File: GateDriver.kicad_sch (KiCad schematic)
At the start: 9 parts, among them U2 UP1966E

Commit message: added license and almost ready for prod
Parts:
- C38, C39: Rating (none) -> 100V
- C40: Rating (none) -> 6.3V
- R1, R2, R4, R5, R8: Rating (none) -> 100mW
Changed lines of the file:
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@@
+			)
+		)
+		(property "Rating" "100mW"
+			(at 151.13 60.96 0)
+			(effects
+				(font
+					(size 1.27 1.27)
+				)
+				(hide yes)
 			)
 		)
@@
 			)
 		)
+		(property "Rating" "100V"
+			(at 176.53 66.04 0)
+			(effects
+				(font
+					(size 1.27 1.27)
+				)
+				(hide yes)
+			)
+		)
 		(pin "2"
 		)
@@
 		)
 		(property "Description" "Resistor, US symbol"
+			(at 81.28 63.5 0)
+			(effects
+				(font
+					(size 1.27 1.27)
+				)
+				(hide yes)
+			)
+		)
+		(property "Rating" "100mW"
 			(at 81.28 63.5 0)
 			(effects
@@
 			)
 		)
+		(property "Rating" ""
+			(at 92.71 73.66 0)
+			(effects
+				(font
+					(size 1.27 1.27)
+				)
+				(hide yes)
+			)
+		)
 		(pin "A3"
 		)
@@
 			)
 		)
+		(property "Rating" "100V"
+			(at 58.42 72.39 0)
+			(effects
+				(font
+					(size 1.27 1.27)
+				)
+				(hide yes)
+			)
+		)
 		(pin "2"
 		)
@@
 			)
 		)
+		(property "Rating" "100mW"
+			(at 82.55 73.66 0)
+			(effects
+				(font
+					(size 1.27 1.27)
+				)
+				(hide yes)
+			)
+		)
 		(pin "2"
 		)
@@
 		)
 		(property "Description" "Resistor, US symbol"
+			(at 143.51 66.04 0)
+			(effects
+				(font
+					(size 1.27 1.27)
+				)
+				(hide yes)
+			)
+		)
+		(property "Rating" "100mW"
 			(at 143.51 66.04 0)
 			(effects
@@
 			)
 		)
+		(property "Rating" "6.3V"
+			(at 44.45 72.39 0)
+			(effects
+				(font
+					(size 1.27 1.27)
+				)
+				(hide yes)
+			)
+		)
 		(pin "2"
 		)
@@
 			(at 146.05 68.58 0)
 			(effects
+				(font
+					(size 1.27 1.27)
+				)
+				(hide yes)
+			)
+		)
+		(property "Rating" "100mW"
+			(at 146.05 68.58 0)
+			(effects

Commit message: first fab run
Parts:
- C38, C39: Manufacturer_Part_Number (none) -> CGA0603X7R104K500JT; Rating 100V -> 6.3V; Source (none) -> LCSC
- C40: Manufacturer_Part_Number (none) -> V475M0603X5R6R3NDT; Source (none) -> LCSC
- R1, R4: value 0 -> 1; Manufacturer_Part_Number (none) -> FRC0603J1R0 TS; Source (none) -> LCSC
- R2, R5, R8: Manufacturer_Part_Number (none) -> SCR0603J0R; Source (none) -> LCSC
- U2: Manufacturer_Part_Number (none) -> UP1966E; Rating (none) -> 85V; Source (none) -> Digikey
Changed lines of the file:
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@@
 		(company "Crab Labs")
 		(comment 1 "Author: Orion Serup")
+		(comment 2 "License: CERN-OHL-W-2.0")
 	)
 	(junction
@@
 			)
 		)
+		(property "Source" "LCSC"
+			(at 151.13 60.96 0)
+			(effects
+				(font
+					(size 1.27 1.27)
+				)
+				(hide yes)
+			)
+		)
+		(property "Manufacturer_Part_Number" "SCR0603J0R"
+			(at 151.13 60.96 0)
+			(effects
+				(font
+					(size 1.27 1.27)
+				)
+				(hide yes)
+			)
+		)
 		(pin "2"
 		)
@@
 			)
 		)
-		(property "Rating" "100V"
+		(property "Rating" "6.3V"
+			(at 176.53 66.04 0)
+			(effects
+				(font
+					(size 1.27 1.27)
+				)
+				(hide yes)
+			)
+		)
+		(property "Source" "LCSC"
+			(at 176.53 66.04 0)
+			(effects
+				(font
+					(size 1.27 1.27)
+				)
+				(hide yes)
+			)
+		)
+		(property "Manufacturer_Part_Number" "CGA0603X7R104K500JT"
 			(at 176.53 66.04 0)
 			(effects
@@
 			)
 		)
-		(property "Value" "0"
+		(property "Value" "1"
 			(at 84.582 61.976 90)
 			(effects
@@
 		)
 		(property "Rating" "100mW"
+			(at 81.28 63.5 0)
+			(effects
+				(font
+					(size 1.27 1.27)
+				)
+				(hide yes)
+			)
+		)
+		(property "Source" "LCSC"
+			(at 81.28 63.5 0)
+			(effects
+				(font
+					(size 1.27 1.27)
+				)
+				(hide yes)
+			)
+		)
+		(property "Manufacturer_Part_Number" "FRC0603J1R0 TS"
 			(at 81.28 63.5 0)
 			(effects
@@
 			)
 		)
-		(property "Rating" ""
+		(property "Rating" "85V"
+			(at 92.71 73.66 0)
+			(effects
+				(font
+					(size 1.27 1.27)
+				)
+				(hide yes)
+			)
+		)
+		(property "Source" "Digikey"
+			(at 92.71 73.66 0)
+			(effects
+				(font
+					(size 1.27 1.27)
+				)
+				(hide yes)
+			)
+		)
+		(property "Manufacturer_Part_Number" "UP1966E"
 			(at 92.71 73.66 0)
 			(effects
@@
 			)
 		)
-		(property "Rating" "100V"
+		(property "Rating" "6.3V"
+			(at 58.42 72.39 0)
+			(effects
+				(font
+					(size 1.27 1.27)
+				)
+				(hide yes)
+			)
+		)
+		(property "Source" "LCSC"
+			(at 58.42 72.39 0)
+			(effects
+				(font
+					(size 1.27 1.27)
+				)
+				(hide yes)
+			)
+		)
+		(property "Manufacturer_Part_Number" "CGA0603X7R104K500JT"
 			(at 58.42 72.39 0)
 			(effects
@@
 			)
 		)
+		(property "Source" "LCSC"
+			(at 82.55 73.66 0)
+			(effects
+				(font
+					(size 1.27 1.27)
+				)
+				(hide yes)
+			)
+		)
+		(property "Manufacturer_Part_Number" "SCR0603J0R"
+			(at 82.55 73.66 0)
+			(effects
+				(font
+					(size 1.27 1.27)
+				)
+				(hide yes)
+			)
+		)
 		(pin "2"
 		)
@@
 			)
 		)
+		(property "Source" "LCSC"
+			(at 143.51 66.04 0)
+			(effects
+				(font
+					(size 1.27 1.27)
+				)
+				(hide yes)
+			)
+		)
+		(property "Manufacturer_Part_Number" "SCR0603J0R"
+			(at 143.51 66.04 0)
+			(effects
+				(font
+					(size 1.27 1.27)
+				)
+				(hide yes)
+			)
+		)
 		(pin "2"
 		)
@@
 		)
 		(property "Rating" "6.3V"
+			(at 44.45 72.39 0)
+			(effects
+				(font
+					(size 1.27 1.27)
+				)
+				(hide yes)
+			)
+		)
+		(property "Manufacturer_Part_Number" "V475M0603X5R6R3NDT"
+			(at 44.45 72.39 0)
+			(effects
+				(font
+					(size 1.27 1.27)
+				)
+				(hide yes)
+			)
+		)
+		(property "Source" "LCSC"
 			(at 44.45 72.39 0)
 			(effects
@@
 			)
 		)
-		(property "Value" "0"
+		(property "Value" "1"
 			(at 150.114 67.056 90)
 			(effects
@@
 			(at 146.05 68.58 0)
 			(effects
+				(font
+					(size 1.27 1.27)
+				)
+				(hide yes)
+			)
+		)
+		(property "Source" "LCSC"
+			(at 146.05 68.58 0)
+			(effects
+				(font
+					(size 1.27 1.27)
+				)
+				(hide yes)
+			)
+		)
+		(property "Manufacturer_Part_Number" "FRC0603J1R0 TS"
+			(at 146.05 68.58 0)
+			(effects

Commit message: added ESD protection
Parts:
- added D12, D15: 100V, Diode_SMD:D_0603_1608Metric, symbol Device:D_TVS_Small
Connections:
- net GND: now also D12.1 (A1), D15.1 (A1)
- net HIGH_IN: now also D12.2 (A2)
- net LOW_IN: now also D15.2 (A2)

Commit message: added all changes from Reddit
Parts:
- D13: renamed from D12; value 100V -> 5V
- D16: renamed from D15; value 100V -> 5V
- renumbered C38 to C41, C39 to C42, R5 to R10, R1 to R6, R2 to R7, R4 to R9
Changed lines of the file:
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@@
 		(on_board yes)
 		(dnp no)
-		(property "Reference" "R5"
+		(property "Reference" "R10"
 			(at 150.876 58.42 90)
 			(effects
@@
 		(dnp no)
 		(fields_autoplaced yes)
-		(property "Reference" "D15"
+		(property "Reference" "D16"
 			(at 59.69 50.7999 90)
 			(effects
@@
 			)
 		)
-		(property "Value" "100V"
+		(property "Value" "5V"
 			(at 59.69 53.3399 90)
 			(effects
@@
 		(on_board yes)
 		(dnp no)
-		(property "Reference" "C39"
+		(property "Reference" "C42"
 			(at 181.864 64.516 0)
 			(effects
@@
 		(dnp no)
 		(fields_autoplaced yes)
-		(property "Reference" "D12"
+		(property "Reference" "D13"
 			(at 45.72 50.7999 90)
 			(effects
@@
 			)
 		)
-		(property "Value" "100V"
+		(property "Value" "5V"
 			(at 45.72 53.3399 90)
 			(effects
@@
 		(on_board yes)
 		(dnp no)
-		(property "Reference" "R1"
+		(property "Reference" "R6"
 			(at 81.026 60.96 90)
 			(effects
@@
 		(dnp no)
 		(fields_autoplaced yes)
-		(property "Reference" "C38"
+		(property "Reference" "C41"
 			(at 62.23 71.1199 0)
 			(effects
@@
 		(on_board yes)
 		(dnp no)
-		(property "Reference" "R2"
+		(property "Reference" "R7"
 			(at 78.486 74.93 90)
 			(effects
@@
 		(on_board yes)
 		(dnp no)
-		(property "Reference" "R4"
+		(property "Reference" "R9"
 			(at 141.986 69.85 90)
 			(effects

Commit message: updates to make better
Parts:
- D13, D16: Manufacturer_Part_Number ULCE1005A015FR -> 0603ESDA-05N
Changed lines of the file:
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@@
 			)
 		)
-		(property "Manufacturer_Part_Number" "ULCE1005A015FR"
+		(property "Manufacturer_Part_Number" "0603ESDA-05N"
 			(at 57.15 52.07 0)
 			(effects
@@
 			)
 		)
-		(property "Manufacturer_Part_Number" "ULCE1005A015FR"
-			(at 43.18 52.07 0)
-			(effects
+		(property "Manufacturer_Part_Number" "0603ESDA-05N"
+			(at 43.18 52.07 0)
+			(effects

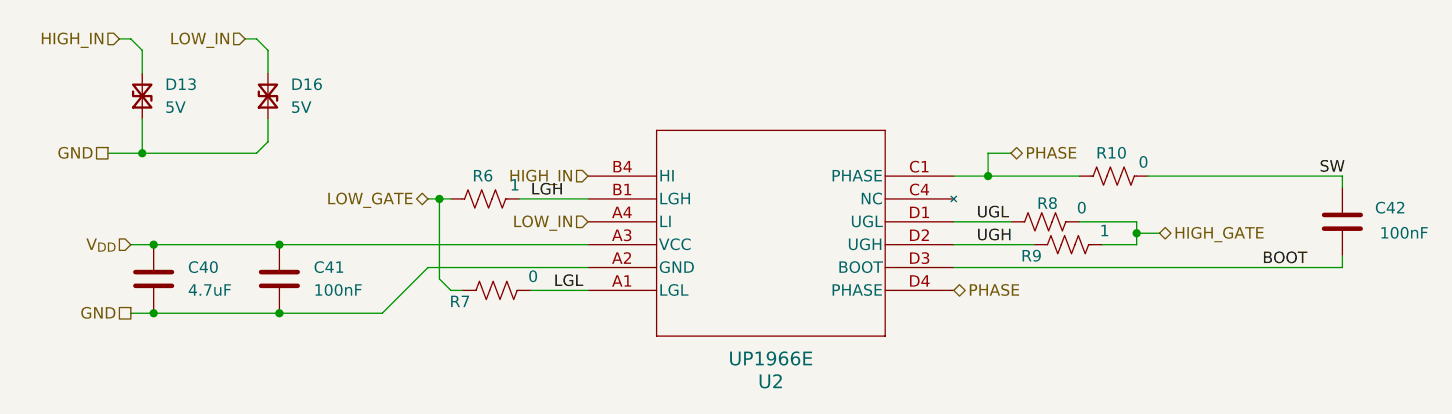
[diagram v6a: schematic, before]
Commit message: moved amps to back
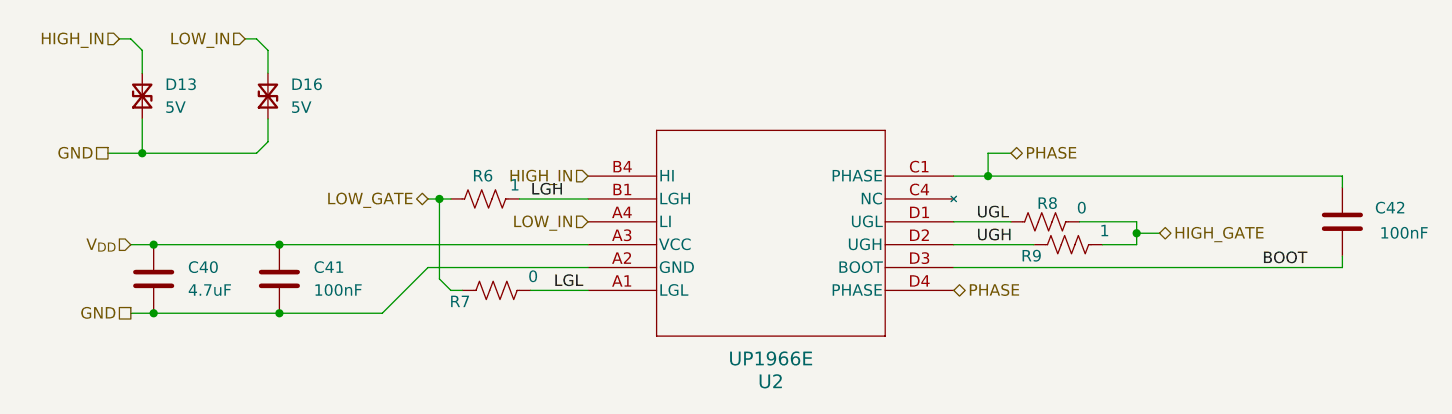
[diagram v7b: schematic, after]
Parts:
- removed R10: 0, Resistor_SMD:R_0603_1608Metric, symbol Device:R_US
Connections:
- net SW is gone; now on net PHASE: C42.2
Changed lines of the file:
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@@
 	(wire
 		(pts
-			(xy 137.16 60.96) (xy 147.32 60.96)
+			(xy 137.16 60.96) (xy 176.53 60.96)
 		)
 		(stroke
@@
 		(pts
 			(xy 142.24 68.58) (xy 133.35 68.58)
-		)
-		(stroke
-			(width 0)
-			(type default)
-		)
-	)
-	(wire
-		(pts
-			(xy 154.94 60.96) (xy 176.53 60.96)
 		)
 		(stroke
@@
 	(label "BOOT"
 		(at 167.64 71.12 0)
-		(fields_autoplaced yes)
-		(effects
-			(font
-				(size 1.27 1.27)
-			)
-			(justify left bottom)
-		)
-	)
-	(label "SW"
-		(at 173.99 60.96 0)
 		(fields_autoplaced yes)
 		(effects
@@
 		)
 	)
-	(symbol
-		(lib_id "Device:R_US")
-		(at 151.13 60.96 270)
-		(unit 1)
-		(exclude_from_sim no)
-		(in_bom yes)
-		(on_board yes)
-		(dnp no)
-		(property "Reference" "R10"
-			(at 150.876 58.42 90)
-			(effects
-				(font
-					(size 1.27 1.27)
-				)
-			)
-		)
-		(property "Value" "0"
-			(at 154.432 59.436 90)
-			(effects
-				(font
-					(size 1.27 1.27)
-				)
-			)
-		)
-		(property "Footprint" "Resistor_SMD:R_0603_1608Metric"
-			(at 150.876 61.976 90)
-			(effects
-				(font
-					(size 1.27 1.27)
-				)
-				(hide yes)
-			)
-		)
-		(property "Datasheet" "~"
-			(at 151.13 60.96 0)
-			(effects
-				(font
-					(size 1.27 1.27)
-				)
-				(hide yes)
-			)
-		)
-		(property "Description" "Resistor, US symbol"
-			(at 151.13 60.96 0)
-			(effects
-				(font
-					(size 1.27 1.27)
-				)
-				(hide yes)
-			)
-		)
-		(property "Rating" "100mW"
-			(at 151.13 60.96 0)
-			(effects
-				(font
-					(size 1.27 1.27)
-				)
-				(hide yes)
-			)
-		)
-		(property "Source" "LCSC"
-			(at 151.13 60.96 0)
-			(effects
-				(font
-					(size 1.27 1.27)
-				)
-				(hide yes)
-			)
-		)
-		(property "Manufacturer_Part_Number" "SCR0603J0R"
-			(at 151.13 60.96 0)
-			(effects
-				(font
-					(size 1.27 1.27)
-				)
-				(hide yes)
-			)
-		)
-		(pin "2"
-		)
-		(pin "1"
-		)
-		(instances
-			(project "OpenMD"
-				(path "/28611c8e-7644-4a1a-8c07-dc86cafc8f6c/088add4a-41d7-49b4-99cc-9239cd70693b/c2de4369-e1cf-48b7-9260-54fc6f5ddd69"
-					(reference "R10")
-					(unit 1)
-				)
-				(path "/28611c8e-7644-4a1a-8c07-dc86cafc8f6c/088add4a-41d7-49b4-99cc-9239cd70693b/cbf4e12a-3fd7-44b5-8509-c83b124ff905"
-					(reference "R5")
-					(unit 1)
-				)
-				(path "/28611c8e-7644-4a1a-8c07-dc86cafc8f6c/088add4a-41d7-49b4-99cc-9239cd70693b/e841f064-3f02-4c16-b30e-9ec0b7ba7273"
-					(reference "R15")
-					(unit 1)
-				)
-			)
-		)
-	)

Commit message: revision 2
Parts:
- C40, C41, C42: footprint Capacitor_SMD:C_0603_1608Metric -> Capacitor_SMD:C_0402_1005Metric
- D13, D16: footprint Diode_SMD:D_0603_1608Metric -> Diode_SMD:D_0402_1005Metric
- R6, R7, R8, R9: footprint Resistor_SMD:R_0603_1608Metric -> Resistor_SMD:R_0402_1005Metric
- U2: value UP1966E -> LM1205
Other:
- note added: "Substitute withh UP1966 or AD8418, same Footprint"
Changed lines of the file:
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@@
+		)
+	)
+	(text "Substitute withh UP1966 or AD8418, same Footprint\n"
+		(exclude_from_sim no)
+		(at 109.982 44.958 0)
+		(effects
+			(font
+				(size 1.27 1.27)
+			)
 		)
 	)
@@
 			)
 		)
-		(property "Footprint" "Diode_SMD:D_0603_1608Metric"
+		(property "Footprint" "Diode_SMD:D_0402_1005Metric"
 			(at 57.15 52.07 0)
 			(effects
@@
 			)
 		)
-		(property "Footprint" "Capacitor_SMD:C_0603_1608Metric"
+		(property "Footprint" "Capacitor_SMD:C_0402_1005Metric"
 			(at 175.5648 62.23 0)
 			(effects
@@
 			)
 		)
-		(property "Footprint" "Diode_SMD:D_0603_1608Metric"
+		(property "Footprint" "Diode_SMD:D_0402_1005Metric"
 			(at 43.18 52.07 0)
 			(effects
@@
 			)
 		)
-		(property "Footprint" "Resistor_SMD:R_0603_1608Metric"
+		(property "Footprint" "Resistor_SMD:R_0402_1005Metric"
 			(at 81.026 64.516 90)
 			(effects
@@
 			)
 		)
-		(property "Value" "UP1966E"
+		(property "Value" "LM1205"
 			(at 113.03 81.28 0)
 			(effects
@@
 			)
 		)
-		(property "Footprint" "Capacitor_SMD:C_0603_1608Metric"
+		(property "Footprint" "Capacitor_SMD:C_0402_1005Metric"
 			(at 59.3852 76.2 0)
 			(effects
@@
 			)
 		)
-		(property "Footprint" "Resistor_SMD:R_0603_1608Metric"
+		(property "Footprint" "Resistor_SMD:R_0402_1005Metric"
 			(at 82.804 72.644 90)
 			(effects
@@
 			)
 		)
-		(property "Footprint" "Resistor_SMD:R_0603_1608Metric"
+		(property "Footprint" "Resistor_SMD:R_0402_1005Metric"
 			(at 143.764 65.024 90)
 			(effects
@@
 			)
 		)
-		(property "Footprint" "Capacitor_SMD:C_0603_1608Metric"
+		(property "Footprint" "Capacitor_SMD:C_0402_1005Metric"
 			(at 45.4152 76.2 0)
 			(effects
@@
 			)
 		)
-		(property "Footprint" "Resistor_SMD:R_0603_1608Metric"
+		(property "Footprint" "Resistor_SMD:R_0402_1005Metric"
 			(at 146.304 67.564 90)
 			(effects
